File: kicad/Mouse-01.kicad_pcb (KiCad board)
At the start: 2 copper layers, 54 x 62 mm, 89 parts, among them P1 MT-ENC, P2 MT-ENC, P3 Battery_A, P4 Battery_B, P5 SWD, P6 UART, Q1 IRLML6402, Q2 IRFML8244, Q3 IRFML8244, Q4 BSS138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

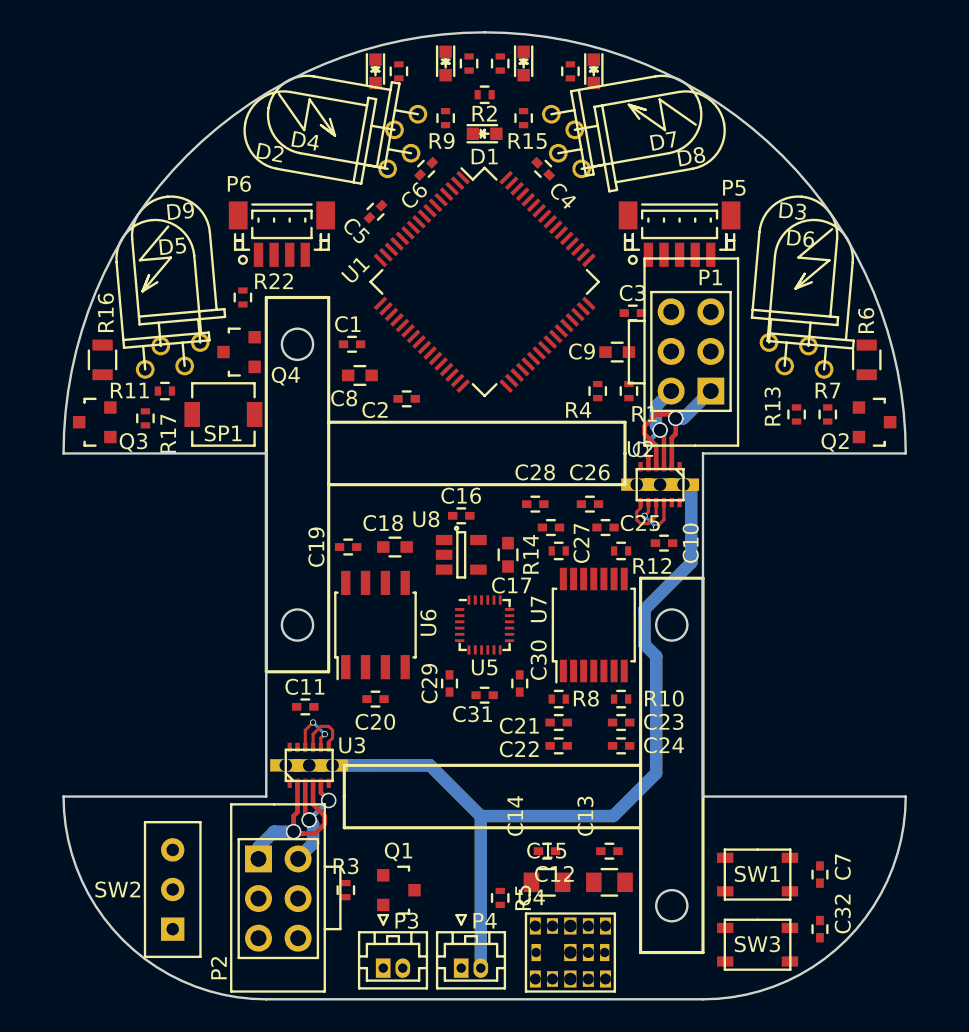
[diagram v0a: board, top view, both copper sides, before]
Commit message: リポ充電基板を追加
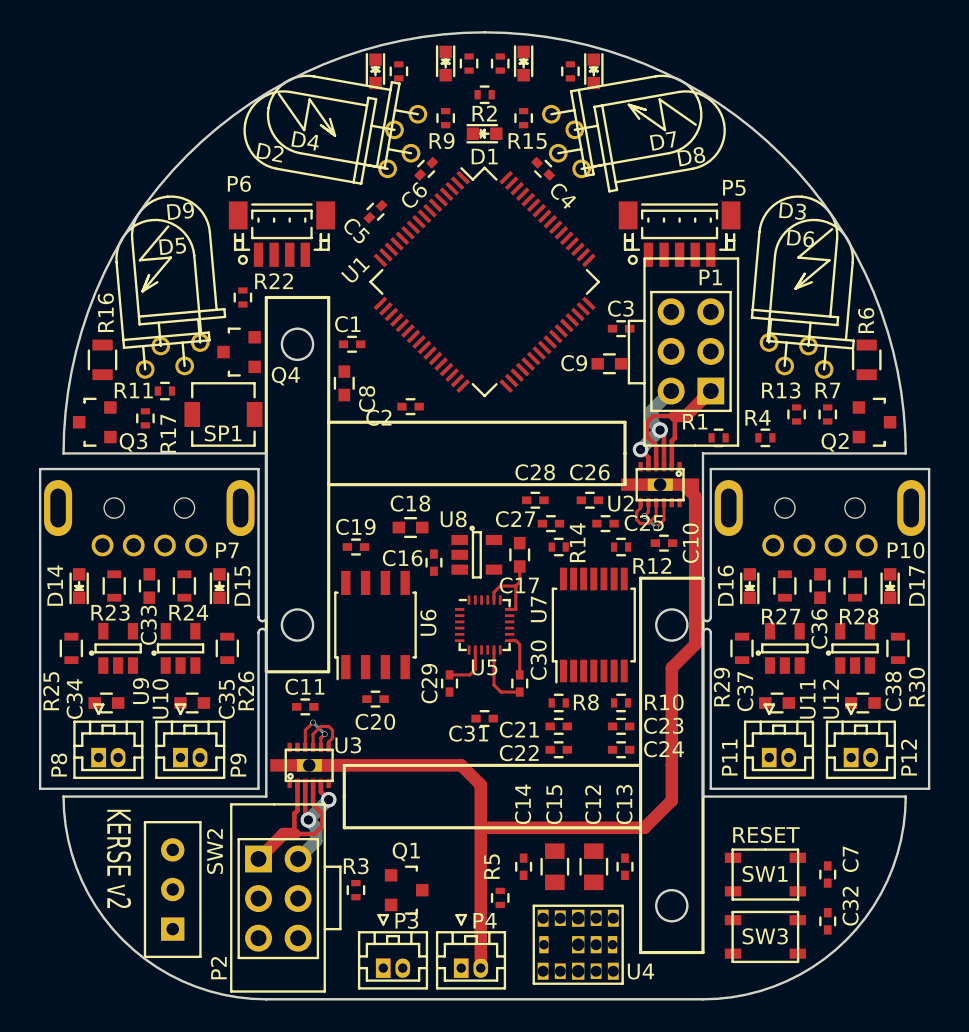
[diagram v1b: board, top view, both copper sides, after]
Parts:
- added C33: 4.7u, Capacitors_SMD:C_0603, F.Cu at (121.5, 131.5)
- added C34: 4.7u, Capacitors_SMD:C_0603, F.Cu at (118.8, 139.0)
- added C35: 4.7u, Capacitors_SMD:C_0603, F.Cu at (124.2, 139.0)
- added C36: 4.7u, Capacitors_SMD:C_0603, F.Cu at (164.5, 131.5)
- added C37: 4.7u, Capacitors_SMD:C_0603, F.Cu at (161.8, 139.0)
- added C38: 4.7u, Capacitors_SMD:C_0603, F.Cu at (167.2, 139.0)
- added D14: LED, LEDs:LED_0603, F.Cu at (117.0, 131.5)
- added D15: LED, LEDs:LED_0603, F.Cu at (126.0, 131.5)
- added D16: LED, LEDs:LED_0603, F.Cu at (160.0, 131.5)
- added D17: LED, LEDs:LED_0603, F.Cu at (169.0, 131.5)
- added G***: LOGO, KERI:KERI_22mm, B.Cu at (143.0, 130.0)
- added P10: USB_A, mouse:USB_A_P, F.Cu at (164.5, 126.5)
- added P11: BAT1, Connectors_Hirose:Hirose_DF13-02P-1.25DSA_02x1.25mm_Straight, F.Cu at (161.2, 142.5)
- added P12: BAT2, Connectors_Hirose:Hirose_DF13-02P-1.25DSA_02x1.25mm_Straight, F.Cu at (166.5, 142.5)
- added P7: USB_A, mouse:USB_A_P, F.Cu at (121.5, 126.5)
- added P8: BAT1, Connectors_Hirose:Hirose_DF13-02P-1.25DSA_02x1.25mm_Straight, F.Cu at (118.2, 142.5)
- added P9: BAT2, Connectors_Hirose:Hirose_DF13-02P-1.25DSA_02x1.25mm_Straight, F.Cu at (123.5, 142.5)
- added R23: 1k, Resistors_SMD:R_0603, F.Cu at (119.2, 131.5)
- added R24: 1k, Resistors_SMD:R_0603, F.Cu at (123.8, 131.5)
- added R25: 4.7k, Resistors_SMD:R_0603, F.Cu at (116.5, 135.5)
- added R26: 4.7k, Resistors_SMD:R_0603, F.Cu at (126.5, 135.5)
- added R27: 1k, Resistors_SMD:R_0603, F.Cu at (162.2, 131.5)
- added R28: 1k, Resistors_SMD:R_0603, F.Cu at (166.8, 131.5)
- added R29: 4.7k, Resistors_SMD:R_0603, F.Cu at (159.5, 135.5)
- added R30: 4.7k, Resistors_SMD:R_0603, F.Cu at (169.5, 135.5)
- added U10: MCP73831, TO_SOT_Packages_SMD:SOT-23-5, F.Cu at (123.5, 135.5)
- added U11: MCP73831, TO_SOT_Packages_SMD:SOT-23-5, F.Cu at (162.2, 135.5)
- added U12: MCP73831, TO_SOT_Packages_SMD:SOT-23-5, F.Cu at (166.8, 135.5)
- added U9: MCP73831, TO_SOT_Packages_SMD:SOT-23-5, F.Cu at (119.5, 135.5)
- moved R4 11.2 mm to (161.0, 122.0), turned to 0 degrees
- moved R1 6.49 mm to (158.0, 122.0), turned to 0 degrees
- moved C16 3.47 mm to (139.8, 130.0), turned to 90 degrees
- moved C14 1.80 mm to (145.5, 149.5), turned to 90 degrees
- moved C18 1.60 mm to (138.2, 127.8)
- moved C31 1.50 mm to (143.0, 140.0)
- moved C12 1.41 mm to (150.0, 149.5), turned to 270 degrees
- moved C13 1.41 mm to (152.0, 149.5), turned to 270 degrees
- moved C3 1.25 mm to (151.8, 115.0)
- moved C15 1.12 mm to (147.5, 149.5), turned to 90 degrees
- moved C8 1.12 mm to (134.0, 118.5), turned to 270 degrees
- moved U5 1.00 mm to (142.5, 129.5)
- moved C9 0.90 mm to (151.0, 117.2)
- moved C17 0.75 mm to (145.2, 129.5)
- moved C32 0.71 mm to (165.0, 153.0)
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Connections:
- net Net-(C31-Pad1) renamed /AXIS_SENSOR/AXIS_CAP
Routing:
- net GND: track 57.9 -> 66.8 mm
- net +3V3: track 0.00 -> 5.75 mm
- net /Motor_R/MT_OUT_1: track 11.8 -> 11.3 mm, vias 1 -> 0
- net /Motor_L/MT_OUT_1: track 11.5 -> 11.4 mm, vias 1 -> 0
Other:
- board size 54 x 62 mm -> 57 x 62 mm
- net class 5V: via_drill 0.4 -> 0.3
- net class AXIS: trace_width 0.2 -> 0.1999; via_dia 0.4 -> 0.36
- net class Default: via_dia 0.4 -> 0.36
- net class GND: via_drill 0.4 -> 0.3
- net class IR_LED: via_drill 0.4 -> 0.3
- net class Motor: via_drill 0.8 -> 0.6
- net class VBAT: via_drill 0.8 -> 0.6
- rule via_min_size: 0.4 -> 0.36
- board text added: "KERISE v2 2016.12.01"
- board text added: "KERSE v2"
- board text removed: "kerikun11 2016.12.01"

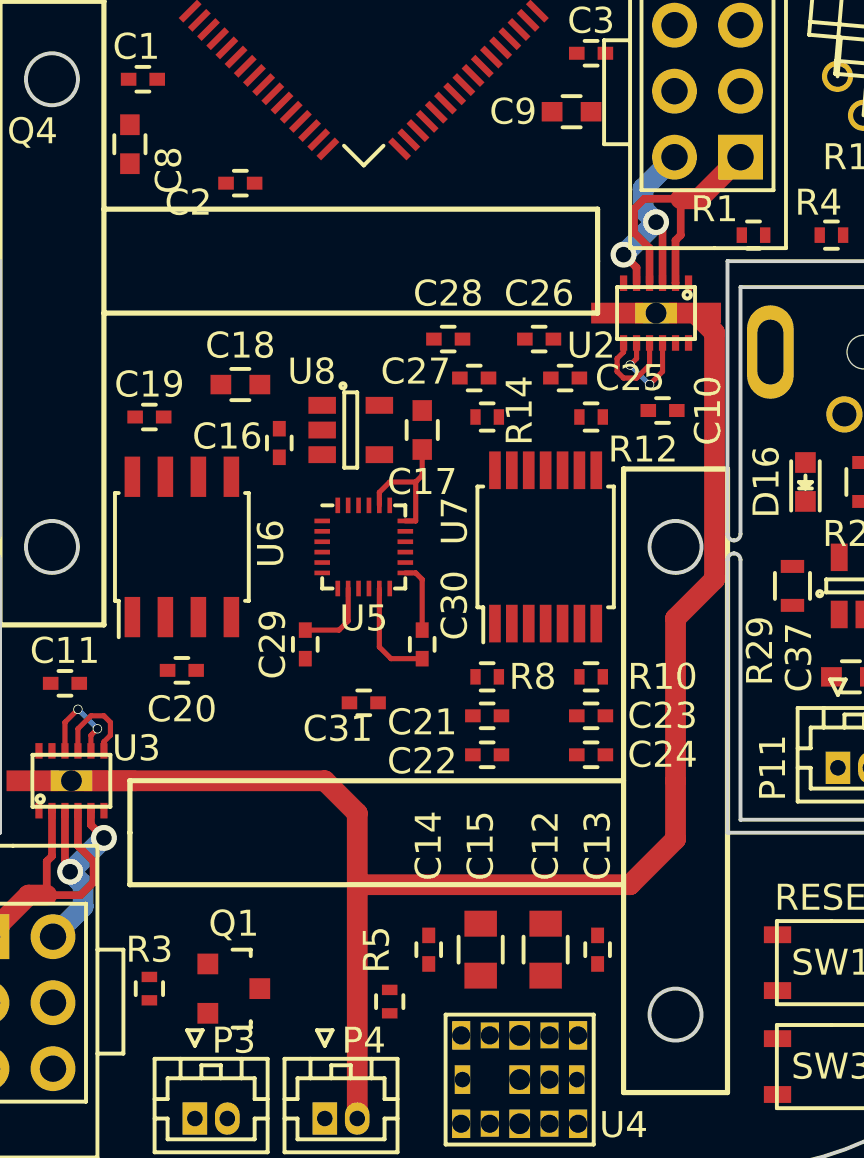
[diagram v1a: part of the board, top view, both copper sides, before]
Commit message: 充電基板を階層に．
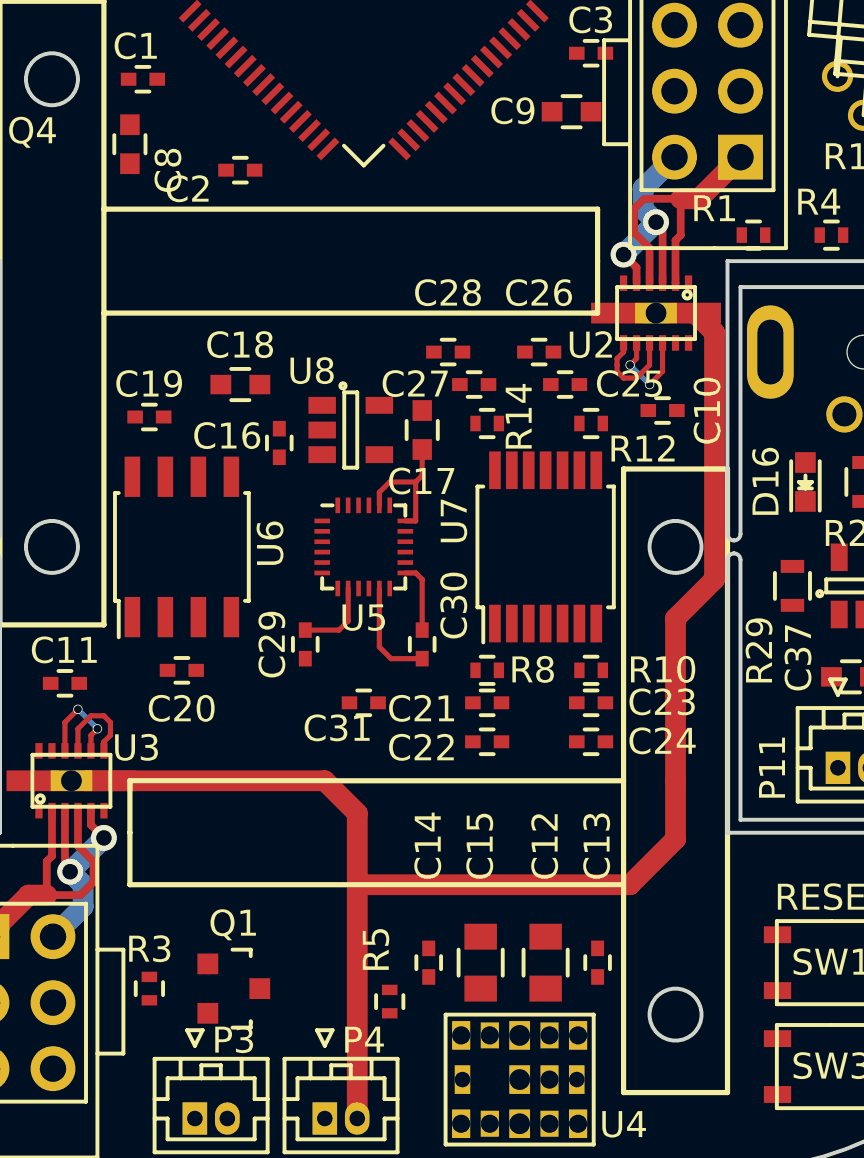
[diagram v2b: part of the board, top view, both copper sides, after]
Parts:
- removed G***: LOGO, KERI:KERI_22mm
- moved C12 0.50 mm to (150.0, 150.0)
- moved C13 0.50 mm to (152.0, 150.0)
- moved C14 0.50 mm to (145.5, 150.0)
- moved C15 0.50 mm to (147.5, 150.0)
- moved C2 0.50 mm to (138.2, 119.5)
- moved C21 0.50 mm to (147.8, 140.0)
- moved C22 0.50 mm to (147.8, 141.5)
- moved C23 0.50 mm to (151.8, 140.0)
- moved C24 0.50 mm to (151.8, 141.5)
- moved C26 0.50 mm to (149.8, 126.5)
- moved C28 0.50 mm to (146.2, 126.5)
- moved C25 0.25 mm to (150.8, 127.8)
- moved C27 0.25 mm to (147.2, 127.8)
- moved R10 0.25 mm to (151.8, 138.8)
- moved R12 0.25 mm to (151.8, 129.2)
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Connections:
- net Net-(C33-Pad1) renamed /Charger A/VDD
- net Net-(C33-Pad2) renamed /Charger A/VSS
- net Net-(C34-Pad1) renamed /Charger A/OUT_1
- net Net-(C35-Pad1) renamed /Charger A/OUT_2
- net Net-(C36-Pad1) renamed /Charger B/VDD
- net Net-(C36-Pad2) renamed /Charger B/VSS
- net Net-(C37-Pad1) renamed /Charger B/OUT_1
- net Net-(C38-Pad1) renamed /Charger B/OUT_2
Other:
- net class Charge added: clearance 0.2, trace_width 0.3999, via_dia 0.5, via_drill 0.3

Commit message: 自動配線Postroute
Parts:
- moved R25 1.41 mm to (115.5, 136.5)
- moved R30 1.41 mm to (170.5, 136.5)
- moved C35 1.35 mm to (123.0, 138.5), turned to 180 degrees
- moved C37 1.35 mm to (163.0, 138.5), turned to 180 degrees
- moved D14 1.12 mm to (116.0, 132.0)
- moved D17 1.12 mm to (170.0, 132.0)
- moved C7 1.00 mm to (165.0, 149.0)
- moved R26 1.00 mm to (126.5, 136.5)
- moved R29 1.00 mm to (159.5, 136.5)
- moved R23 0.90 mm to (118.5, 132.0)
- moved R28 0.90 mm to (167.5, 132.0)
- moved U11 0.75 mm to (163.0, 135.5)
- moved C33 0.71 mm to (121.0, 132.0)
- moved C36 0.71 mm to (165.0, 132.0)
- moved P10 0.71 mm to (165.0, 126.0)
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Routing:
- net /Charger B/VSS: track 0.00 -> 64.4 mm
- net /Charger A/VSS: track 0.00 -> 64.2 mm
- net /Charger B/VDD: track 0.00 -> 24.0 mm
- net /Charger A/VDD: track 0.00 -> 23.6 mm
- net /Charger A/OUT_1: track 0.00 -> 6.33 mm
- net /Charger B/OUT_1: track 0.00 -> 6.33 mm
- net /Charger A/OUT_2: track 0.00 -> 5.79 mm
- net /Charger B/OUT_2: track 0.00 -> 5.79 mm
- net Net-(R28-Pad2): track 0.00 -> 5.67 mm
- net Net-(R24-Pad2): track 0.00 -> 5.67 mm
- net Net-(R26-Pad1): track 0.00 -> 5.01 mm
- net Net-(R30-Pad1): track 0.00 -> 5.01 mm
- net Net-(R23-Pad2): track 0.00 -> 4.65 mm
- net Net-(R27-Pad2): track 0.00 -> 4.18 mm
- net Net-(D15-Pad1): track 0.00 -> 3.49 mm
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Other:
- board size 57 x 62 mm -> 58 x 62 mm

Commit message: 自動配線結果を反映
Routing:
- net GND: track 66.8 -> 384.8 mm, vias 0 -> 4
- net +3V3: track 5.75 -> 153.0 mm, vias 0 -> 7
- net +5V: track 0.00 -> 141.6 mm, vias 0 -> 4
- net +BATT: track 0.00 -> 101.0 mm, vias 0 -> 1
- net +3.3VADC: track 0.00 -> 96.0 mm, vias 0 -> 4
- net RESET: track 0.00 -> 67.7 mm, vias 0 -> 5
- net EN-R-A: track 0.00 -> 57.7 mm, vias 0 -> 2
- net EN-R-B: track 0.00 -> 56.3 mm, vias 0 -> 1
- net BUTTON: track 0.00 -> 52.5 mm, vias 0 -> 2
- net Net-(C22-Pad2): track 0.00 -> 51.1 mm, vias 0 -> 2
- net Net-(C24-Pad2): track 0.00 -> 43.1 mm, vias 0 -> 4
- net PR-RCV-FL: track 0.00 -> 37.9 mm, vias 0 -> 2
- net PR-RCV-SL: track 0.00 -> 36.5 mm, vias 0 -> 2
- net /IR_LED_SL_FR/IR_LED_to_IR_LED: track 0.00 -> 36.3 mm
- net /IR_LED_FL_SR/IR_LED_to_IR_LED: track 0.00 -> 30.0 mm
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
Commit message: viaを量産
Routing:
- net GND: track 384.8 -> 1229.8 mm, vias 4 -> 531
- added copper zone on B.Cu, net GND
- added copper zone on F.Cu, net GND

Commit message: ガーバーを生成
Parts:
- added G***: LOGO, KERI:KERI_25mm, B.Cu at (143.0, 129.0)
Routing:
- net GND: track 1229.8 -> 1236.0 mm, vias 531 -> 536
- added copper zone on B.Cu, net /Charger A/VSS
- added copper zone on F.Cu, net /Charger A/VSS
- added copper zone on B.Cu, net /Charger B/VSS
- added copper zone on F.Cu, net /Charger B/VSS
